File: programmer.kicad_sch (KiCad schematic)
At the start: 0 parts

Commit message: Added a test text
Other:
- note added: "hello world!"
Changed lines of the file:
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@@
 	(generator_version "8.0")
 	(paper "A4")
+	(text "hello world!\n"
+		(exclude_from_sim no)
+		(at 94.234 93.218 0)
+		(effects
+			(font
+				(size 1.27 1.27)
+			)
+		)
+	)
 )

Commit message: progress
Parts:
- added C1: 100nF, Capacitor_SMD:C_0603_1608Metric, symbol Device:C_Polarized_Small_US
- added J1: USB_C_Receptacle, Connector_USB:USB_C_Receptacle_Molex_105450-0101, symbol Connector:USB_C_Receptacle
- added Q1, Q2: BC817, Package_TO_SOT_SMD:SOT-23, symbol Transistor_BJT:BC817
- added R5, R6: 10k, Resistor_SMD:R_0603_1608Metric, symbol Device:R
- added U3: CH340C, Package_SO:SOIC-16_3.9x9.9mm_P1.27mm, symbol Interface_USB:CH340C
- added U4: ESP32-WROOM-32, RF_Module:ESP32-WROOM-32, symbol RF_Module:ESP32-WROOM-32
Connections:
- new net: Q1.1 (B), R6.2
- new net: Q1.2 (E), R5.1, U3.13 (~{DTR})
- new net: Q1.3 (C), U4.25 (IO0)
- new net: Q2.1 (B), R5.2
- new net: Q2.2 (E), R6.1, U3.14 (~{RTS})
- new net: Q2.3 (C), U4.3 (EN)
- new net: J1.A1 (GND), J1.A12 (GND), J1.B1 (GND), J1.B12 (GND)
- new net: J1.A4 (VBUS), J1.A9 (VBUS), J1.B4 (VBUS), J1.B9 (VBUS)
- new net: U4.1 (GND), U4.15 (GND), U4.38 (GND), U4.39 (GND)
- new net +5V: C1.1, U3.16 (VCC)
- new net ESP_RX: U3.2 (TXD), U4.34 (RXD0/IO3)
- new net ESP_TX: U3.3 (RXD), U4.35 (TXD0/IO1)
- new net GND: C1.2
- new net USB_D+: J1.A6 (D+), J1.B6 (D+), U3.15 (R232)
- no-connect marks 0 -> 4
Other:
- note removed: "hello world!"

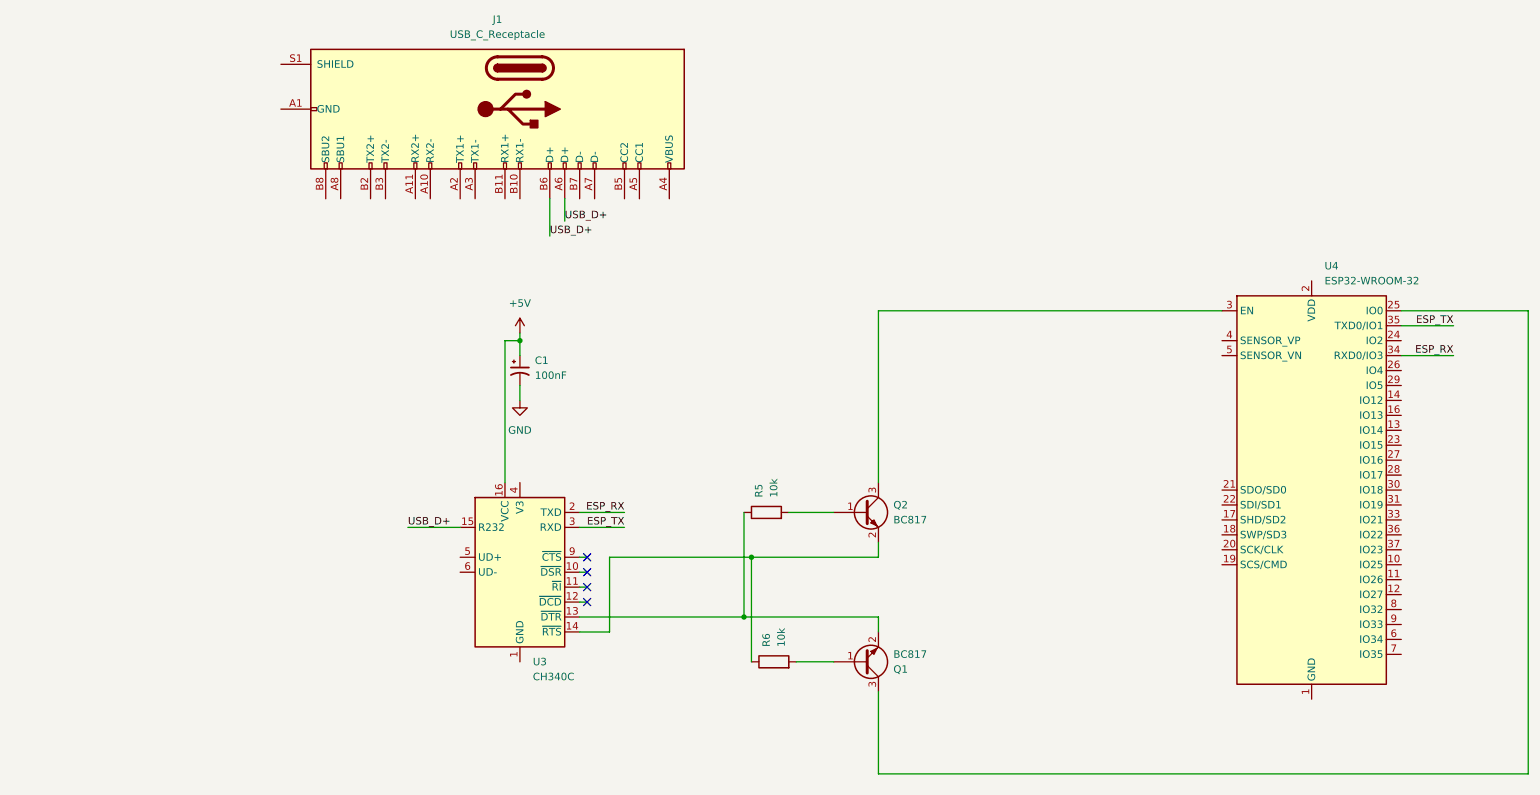
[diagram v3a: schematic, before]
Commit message: pull down resistors included, don't seem necessary so double check
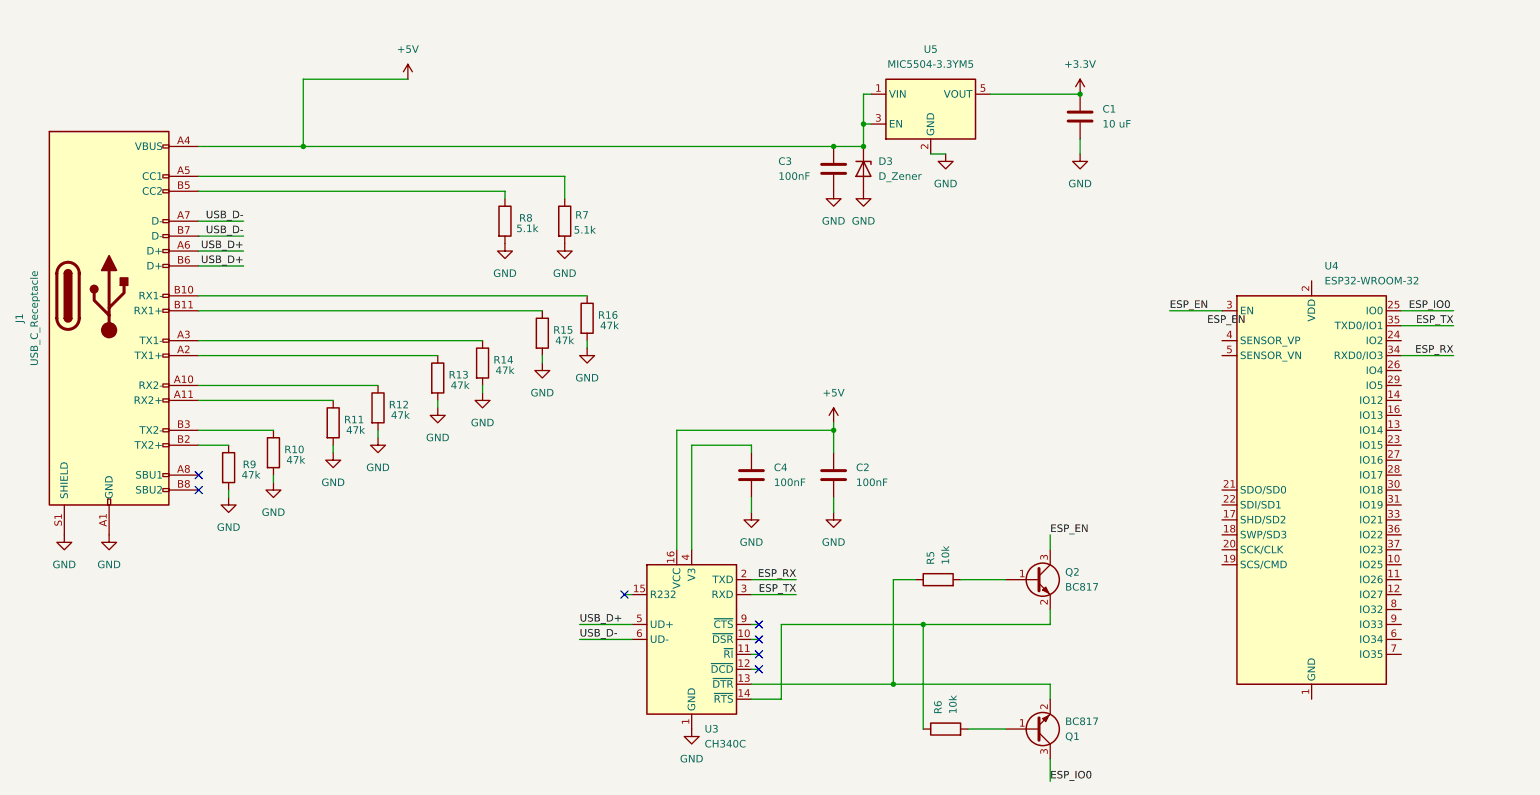
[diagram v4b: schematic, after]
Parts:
- removed C1: 100nF, Capacitor_SMD:C_0603_1608Metric, symbol Device:C_Polarized_Small_US
- added C1: 10 uF, Capacitor_SMD:C_0603_1608Metric, symbol Device:C
- added C2, C3, C4: 100nF, symbol Device:C
- added D3: D_Zener, symbol Device:D_Zener
- added R10, R11, R12, R13, R14, R15, R16, R9: 47k, Resistor_SMD:R_0603_1608Metric, symbol Device:R
- added R7, R8: 5.1k, Resistor_SMD:R_0603_1608Metric, symbol Device:R
- added U5: MIC5504-3.3YM5, Package_TO_SOT_SMD:SOT-23-5, symbol Regulator_Linear:MIC5504-3.3YM5
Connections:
- net +5V: now also J1.A4 (VBUS), J1.A9 (VBUS), J1.B4 (VBUS), J1.B9 (VBUS), C2.1, C3.1, D3.1 (K), U5.1 (VIN), U5.3 (EN)
- net GND: now also J1.A1 (GND), J1.A12 (GND), J1.B1 (GND), J1.B12 (GND), J1.S1 (SHIELD), U3.1 (GND), C1.2, C2.2, C3.2, C4.2, D3.2 (A), R10.2, R11.2, R12.2, R13.2, R14.2, R15.2, R16.2, R7.2, R8.2, R9.2, U5.2 (GND)
- net USB_D+: now also U3.5 (UD+); no longer U3.15 (R232)
- net ESP_IO0: now reaches Q1.3 (C), U4.25 (IO0)
- net ESP_EN: now reaches Q2.3 (C), U4.3 (EN)
- net at U3.4 (V3): now also C4.1
- net USB_D-: now reaches U3.6 (UD-)
- net USB_D-: now also J1.A7 (D-), J1.B7 (D-)
- net at J1.A10 (RX2-): now also R12.1
- net at J1.A11 (RX2+): now also R11.1
- net at J1.A2 (TX1+): now also R13.1
- net at J1.A3 (TX1-): now also R14.1
- net at J1.A5 (CC1): now also R7.1
- net at J1.B10 (RX1-): now also R16.1
- net at J1.B11 (RX1+): now also R15.1
- net at J1.B2 (TX2+): now also R9.1
- net at J1.B3 (TX2-): now also R10.1
- net at J1.B5 (CC2): now also R8.1
- new net +3.3V: C1.1, U5.5 (VOUT)
- no-connect marks 4 -> 7
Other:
- moved on the sheet: J1, Q1, Q2, R5, R6, U3

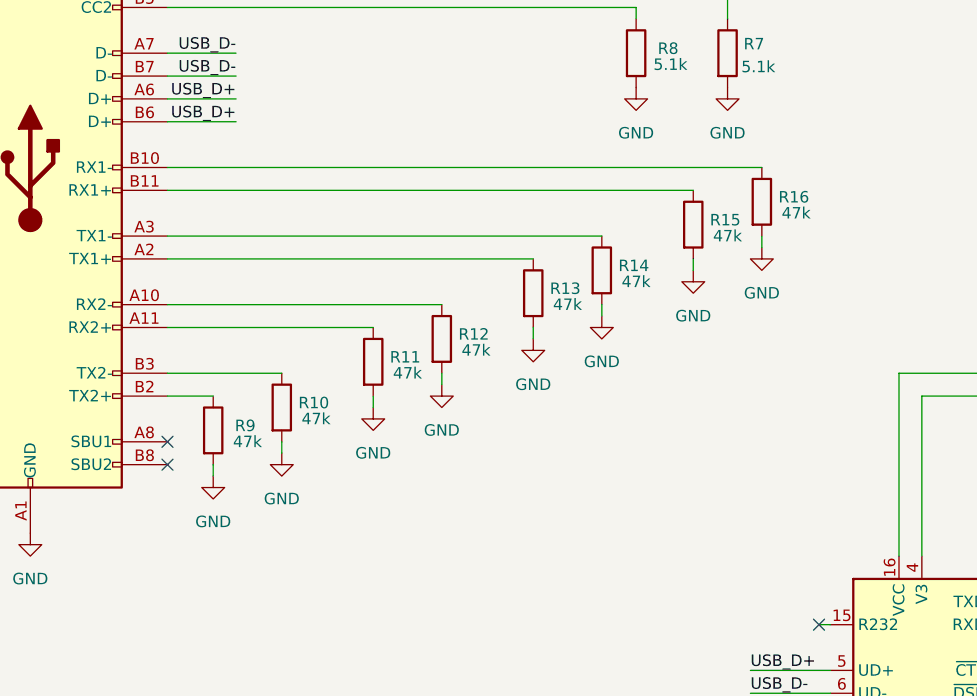
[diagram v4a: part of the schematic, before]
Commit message: don't need pull down for RX and TX. Difficult to route D- and D+ with via's. Can you change line thickness?
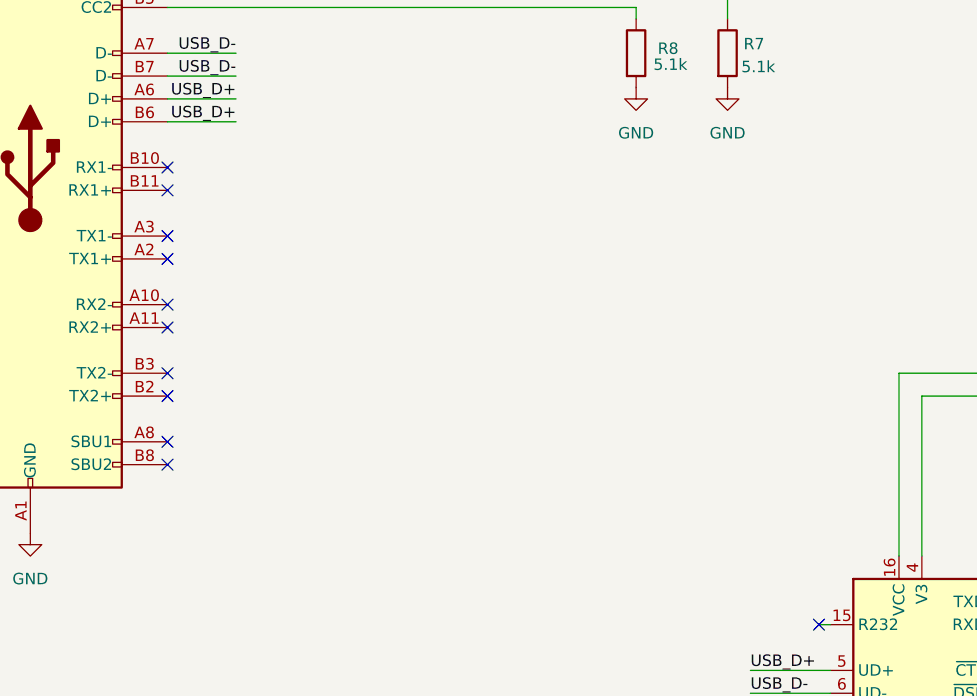
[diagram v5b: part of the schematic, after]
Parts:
- removed R10, R11, R12, R13, R14, R15, R16, R9: 47k, Resistor_SMD:R_0603_1608Metric, symbol Device:R
- D3: footprint (none) -> Package_TO_SOT_SMD:SOT-23
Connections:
- net +5V: now also D3.3 (K); no longer D3.1 (K)
- net GND: now also D3.1 (A); no longer D3.2 (A)
- no-connect marks 7 -> 15

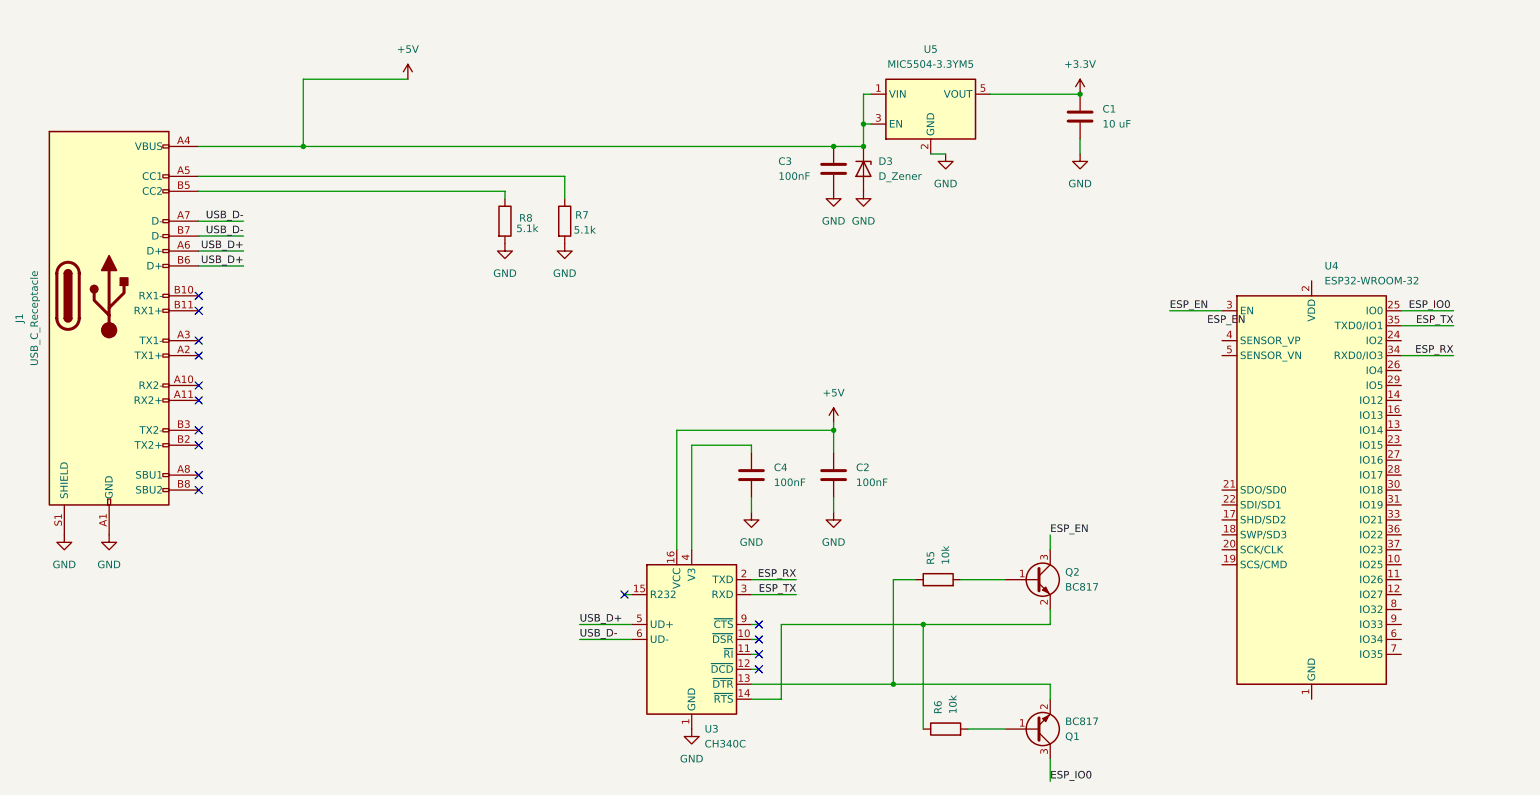
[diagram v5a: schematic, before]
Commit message: One of the 5V is impossible to route. Would having a different type of USB-C connector help?
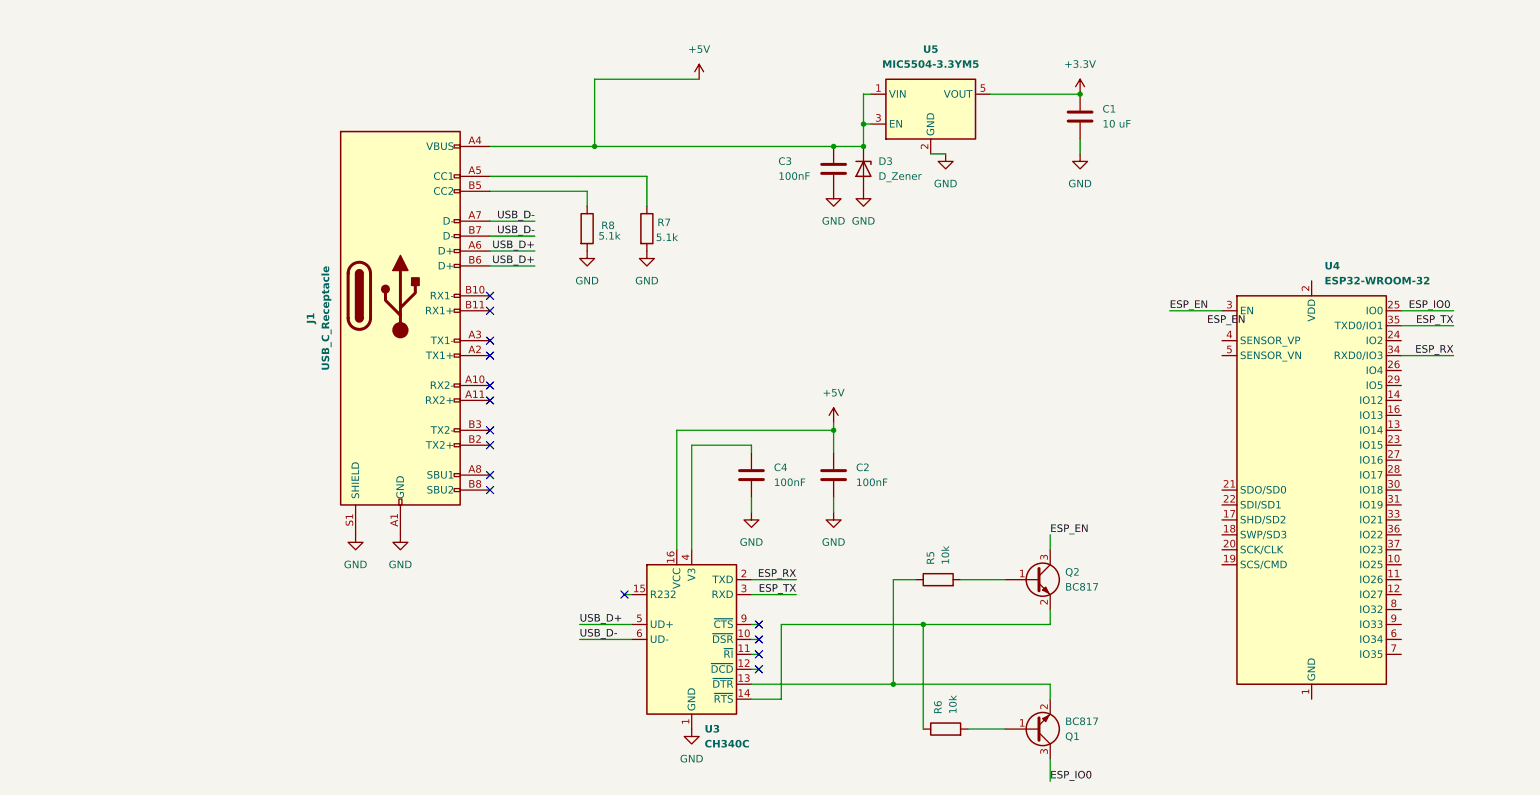
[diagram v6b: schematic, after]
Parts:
- C2, C3, C4: footprint (none) -> Capacitor_SMD:C_0603_1608Metric
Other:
- moved on the sheet: J1, R7, R8

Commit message: the part tags are gone? opened incorrectly?
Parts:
- renumbered C1 to C?, C4 to C?, C3 to C?, C2 to C?, D3 to D?, J1 to J?, Q1 to Q?, Q2 to Q?, R7 to R?, R5 to R?, R6 to R?, R8 to R?, U3 to U?, U5 to U?, U4 to U?
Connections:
- net +3.3V: now also U?.2 (VDD)
- net GND: now also U?.1 (GND), U?.15 (GND), U?.38 (GND), U?.39 (GND)

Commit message: names are fixed
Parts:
- gave numbers to parts that had none: 15
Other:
- moved on the sheet: C2, D1
